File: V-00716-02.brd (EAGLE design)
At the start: 63 x 43 mm, 21 parts, among them Q1 14.74MHz, U1 ATMEGA32U2-AU, X1 MINI-USB-32005-201

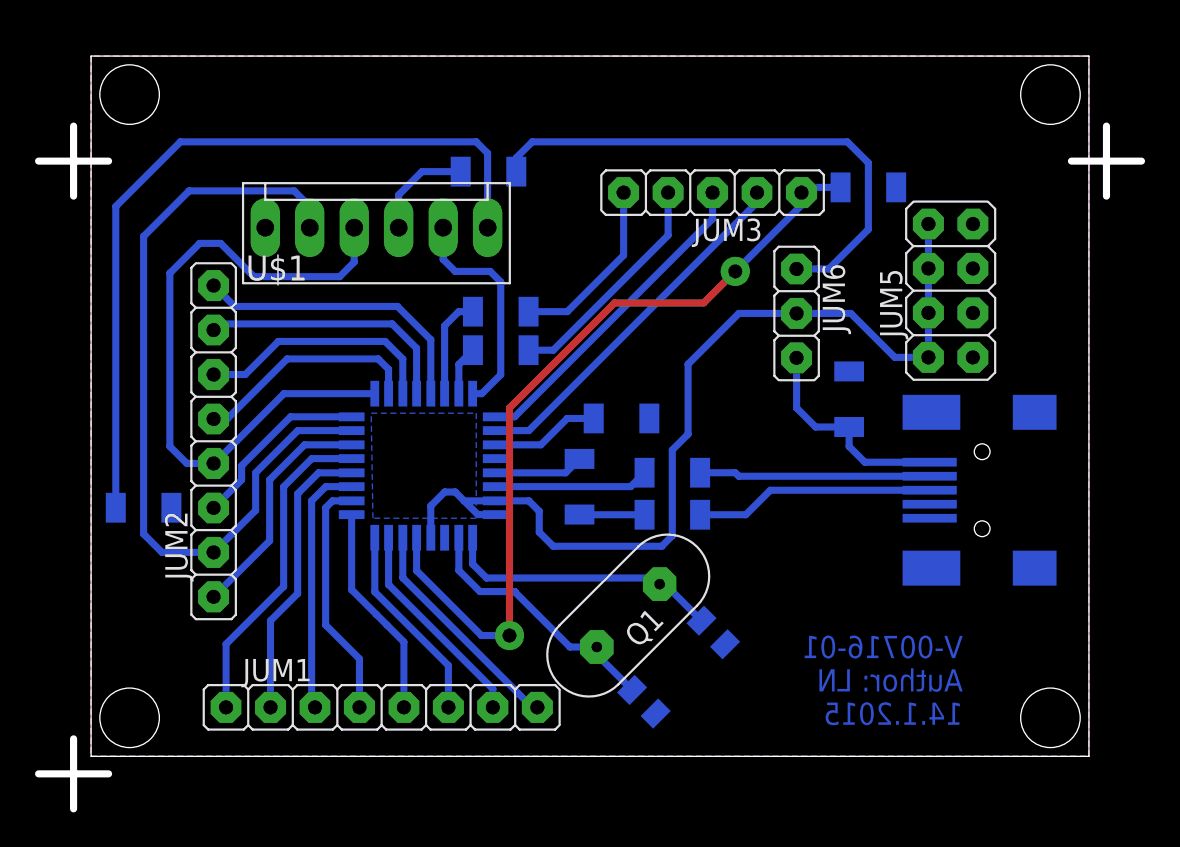
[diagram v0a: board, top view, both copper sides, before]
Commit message: v.2.1
Upravena verze + udelana verze 02 s upravy chyb
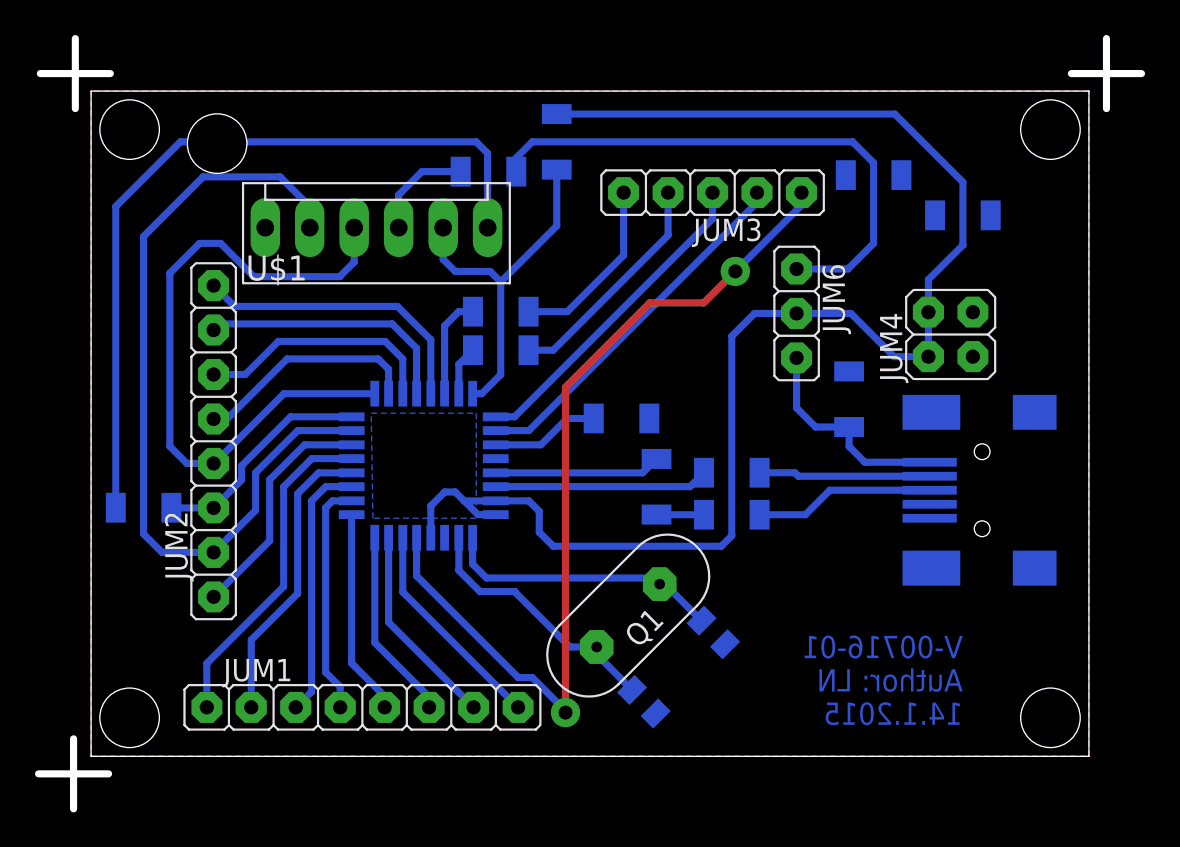
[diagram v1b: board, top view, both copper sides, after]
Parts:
- removed JUM5: S2G4_JUMP, #PaJa_konektory:S2G4_JUM
- added JUM4: S2G2_JUMP, #PaJa_konektory:S2G2_JUM
- added R10: 0R, #PaJa_31:1206
- added R9: 10k, #PaJa_31:1206
- moved R7 4.40 mm to (32.3, 15.4)
- moved R5 3.40 mm to (36.6, 13.8)
- moved R8 3.40 mm to (36.6, 16.2)
- moved JUM1 1.10 mm to (15.5, 2.80)
- moved R6 0.76 mm to (44.7, 33.2)
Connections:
- net +5V: now also JUM4.2_1, JUM4.2_2, R9.2; no longer JUM5.2_1, JUM5.2_2, JUM5.2_3, JUM5.2_4
- net GNDINT: now also JUM4.1_1, JUM4.1_2, R10.1, R10.2, R6.1, R6.2; no longer JUM5.1_1, JUM5.1_2, JUM5.1_3, JUM5.1_4
- net N$10: no longer R6.1, R6.2
- net RESET: now also R9.1
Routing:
- net +5V: track 54.1 -> 83.5 mm
- net RESET: track 13.0 -> 20.7 mm
- net N$10: track 46.3 -> 51.5 mm
- net N$2: track 5.11 -> 9.51 mm
- net DATA+: track 17.4 -> 13.0 mm
- net N$12: track 8.83 -> 12.2 mm
- net DATA-: track 13.2 -> 9.80 mm
- net P_MOSI: track 55.0 -> 57.4 mm
- net +5V_P: track 36.6 -> 37.6 mm
- net P_SCK: track 45.6 -> 46.3 mm
- net N$9: track 13.0 -> 12.4 mm
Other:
- board size 63 x 43 mm -> 63 x 44 mm
